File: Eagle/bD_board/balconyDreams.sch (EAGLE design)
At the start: 35 parts, among them IC1 7805L, Q1 2N7002, Q2 2N7002, Q3 2N7002, Q4 2N7002, Q5 2N7002, Q6 2N7002, Q7 2N7002, Q8 2N7002, U1 MKR1000, X2 MKDSN1,5/2-5,08

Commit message: Lots of stuff - ready for review
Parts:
- added C2: 0.33uF, rcl:CPOL-EUE5-6
- added D1, D2, D3, D4, D5, D6, D7: (no value), diode:DIODE-SOD323-W
- added LED1, LED2, LED3: (no value), led:LEDCHIPLED_0805
- added Q10, Q11, Q9: 2N7002, transistors_gaui:2N7002
- added R16, R18, R20: 10k, rcl:R-EU_R0805
- added R17, R19, R21: 330R, rcl:R-EU_R0805
- C1: value (none) -> 1uF
- IC1: value 7805L -> 7805TV; device linear:7805L -> linear:7805TV
- R10, R11, R12, R13, R14, R15, R8, R9: value (none) -> 10k
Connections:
- new net LED1: Q9.G, R16.1, U1.GPIO9/SCK
- new net LED2: Q10.G, R18.1, U1.GPIO10/MISO
- new net LED3: Q11.G, R20.1, U1.GPIO11/SDA
- new net N$1: LED1.C, R17.1
- new net N$2: Q9.D, R17.2
- new net N$3: Q10.D, R19.2
- new net N$4: LED2.C, R19.1
- new net N$5: Q11.D, R21.2
- new net N$6: LED3.C, R21.1
- net A0: now also D1.C
- net A1: now also D2.C
- net A2: now also D3.C
- net A3: now also D4.C
- net A4: now also D5.C
- net A5: now also D6.C
- net A6: now also D7.C
- net GND: now also C2.-, D1.A, D2.A, D3.A, D4.A, D5.A, D6.A, D7.A, Q10.S, Q11.S, Q9.S, R16.2, R18.2, R20.2
- net VCC: now also LED1.A, LED2.A, LED3.A
- net V_INPUT: now also C2.+
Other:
- note added: "5V level shifter for relais"
- note added: "5V linear regulator"
- note added: "LEDs"
- note added: "MKR 1000 Arduino"
- note added: "connection to 8 Relay Module"
- note added: "connector for soil moisture probes"
- note added: "power connector (7-30V)"
- moved on the sheet: C1, IC1, Q1, Q2, Q3, Q4, Q5, Q6, Q7, Q8, R1, R10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

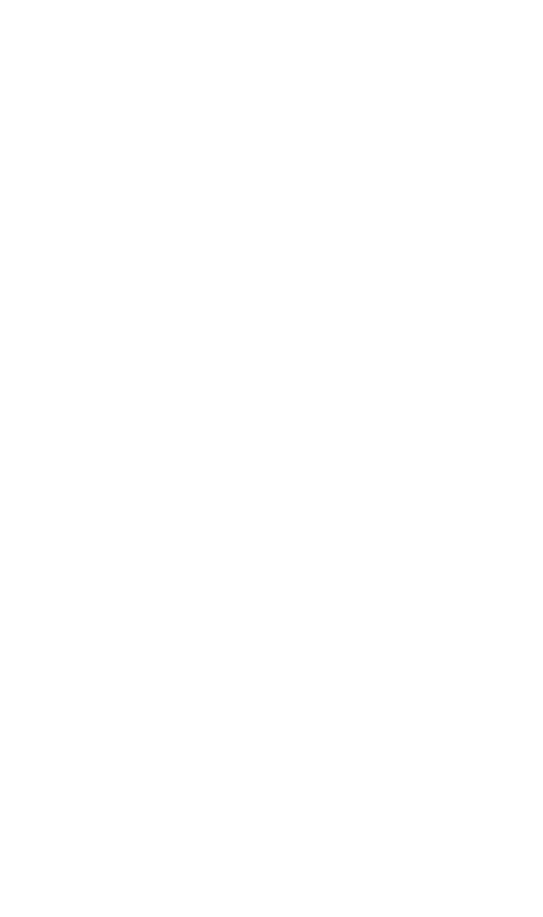
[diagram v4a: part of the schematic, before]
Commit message: add GND connectors for valves
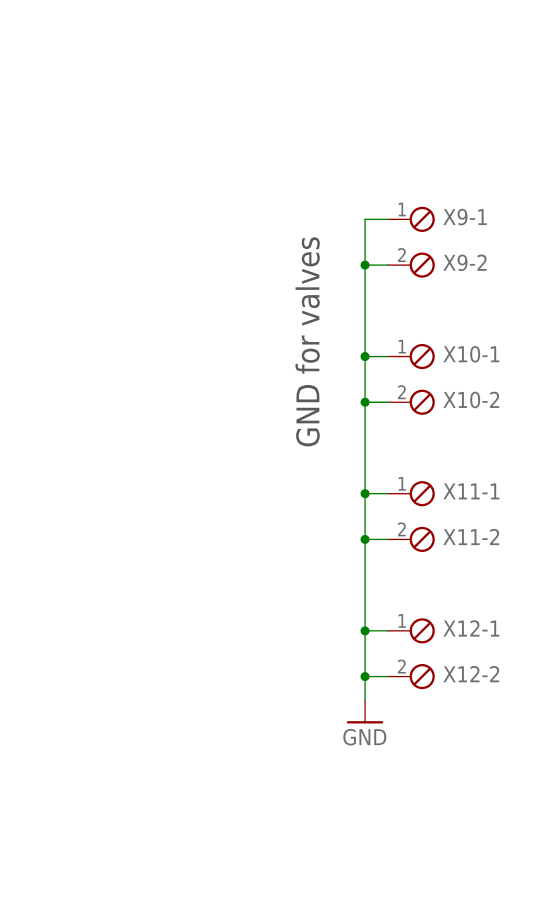
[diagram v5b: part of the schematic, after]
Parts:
- added X10, X11, X12, X9: (no value), con-phoenix-254:MPT2
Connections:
- net GND: now also X10-1.1, X10-2.1, X11-1.1, X11-2.1, X12-1.1, X12-2.1, X9-1.1, X9-2.1
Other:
- note added: "GND for valves"
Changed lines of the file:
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@@
 <part name="GND34" library="supply1" deviceset="GND" device=""/>
 <part name="FRAME1" library="frames" deviceset="DINA3_L" device=""/>
+<part name="X9" library="con-phoenix-254" deviceset="MPT2" device=""/>
+<part name="X10" library="con-phoenix-254" deviceset="MPT2" device=""/>
+<part name="X11" library="con-phoenix-254" deviceset="MPT2" device=""/>
+<part name="X12" library="con-phoenix-254" deviceset="MPT2" device=""/>
+<part name="GND38" library="supply1" deviceset="GND" device=""/>
 </parts>
 <sheets>
@@
 <text x="30.48" y="104.14" size="2.54" layer="97">5V linear regulator</text>
 <text x="33.02" y="35.56" size="2.54" layer="97">power connector (7-30V)</text>
+<text x="353.06" y="134.62" size="2.54" layer="97" rot="R90">GND for valves</text>
 </plain>
 <instances>
@@
 <instance part="FRAME1" gate="G$1" x="0" y="0"/>
 <instance part="FRAME1" gate="G$2" x="287.02" y="0"/>
+<instance part="X9" gate="-1" x="363.22" y="160.02"/>
+<instance part="X9" gate="-2" x="363.22" y="154.94"/>
+<instance part="X10" gate="-1" x="363.22" y="144.78"/>
+<instance part="X10" gate="-2" x="363.22" y="139.7"/>
+<instance part="X11" gate="-1" x="363.22" y="129.54"/>
+<instance part="X11" gate="-2" x="363.22" y="124.46"/>
+<instance part="X12" gate="-1" x="363.22" y="114.3"/>
+<instance part="X12" gate="-2" x="363.22" y="109.22"/>
+<instance part="GND38" gate="1" x="358.14" y="104.14"/>
 </instances>
 <busses>
@@
 <wire x1="40.64" y1="78.74" x2="40.64" y2="81.28" width="0.1524" layer="91"/>
 </segment>
+<segment>
+<pinref part="GND38" gate="1" pin="GND"/>
+<pinref part="X12" gate="-2" pin="1"/>
+<wire x1="358.14" y1="106.68" x2="358.14" y2="109.22" width="0.1524" layer="91"/>
+<wire x1="358.14" y1="109.22" x2="360.68" y2="109.22" width="0.1524" layer="91"/>
+<pinref part="X12" gate="-1" pin="1"/>
+<wire x1="360.68" y1="114.3" x2="358.14" y2="114.3" width="0.1524" layer="91"/>
+<wire x1="358.14" y1="114.3" x2="358.14" y2="109.22" width="0.1524" layer="91"/>
+<junction x="358.14" y="109.22"/>
+<pinref part="X11" gate="-2" pin="1"/>
+<wire x1="358.14" y1="124.46" x2="360.68" y2="124.46" width="0.1524" layer="91"/>
+<wire x1="358.14" y1="124.46" x2="358.14" y2="114.3" width="0.1524" layer="91"/>
+<junction x="358.14" y="114.3"/>
+<pinref part="X11" gate="-1" pin="1"/>
+<wire x1="360.68" y1="129.54" x2="358.14" y2="129.54" width="0.1524" layer="91"/>
+<wire x1="358.14" y1="129.54" x2="358.14" y2="124.46" width="0.1524" layer="91"/>
+<junction x="358.14" y="124.46"/>
+<pinref part="X10" gate="-2" pin="1"/>
+<wire x1="358.14" y1="139.7" x2="360.68" y2="139.7" width="0.1524" layer="91"/>
+<wire x1="358.14" y1="139.7" x2="358.14" y2="129.54" width="0.1524" layer="91"/>
+<junction x="358.14" y="129.54"/>
+<pinref part="X10" gate="-1" pin="1"/>
+<wire x1="360.68" y1="144.78" x2="358.14" y2="144.78" width="0.1524" layer="91"/>
+<wire x1="358.14" y1="144.78" x2="358.14" y2="139.7" width="0.1524" layer="91"/>
+<junction x="358.14" y="139.7"/>
+<pinref part="X9" gate="-2" pin="1"/>
+<wire x1="358.14" y1="154.94" x2="360.68" y2="154.94" width="0.1524" layer="91"/>
+<wire x1="358.14" y1="154.94" x2="358.14" y2="144.78" width="0.1524" layer="91"/>
+<junction x="358.14" y="144.78"/>
+<pinref part="X9" gate="-1" pin="1"/>
+<wire x1="360.68" y1="160.02" x2="358.14" y2="160.02" width="0.1524" layer="91"/>
+<wire x1="358.14" y1="160.02" x2="358.14" y2="154.94" width="0.1524" layer="91"/>
+<junction x="358.14" y="154.94"/>
+</segment>
 </net>
